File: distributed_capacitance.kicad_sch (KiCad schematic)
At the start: 22 parts

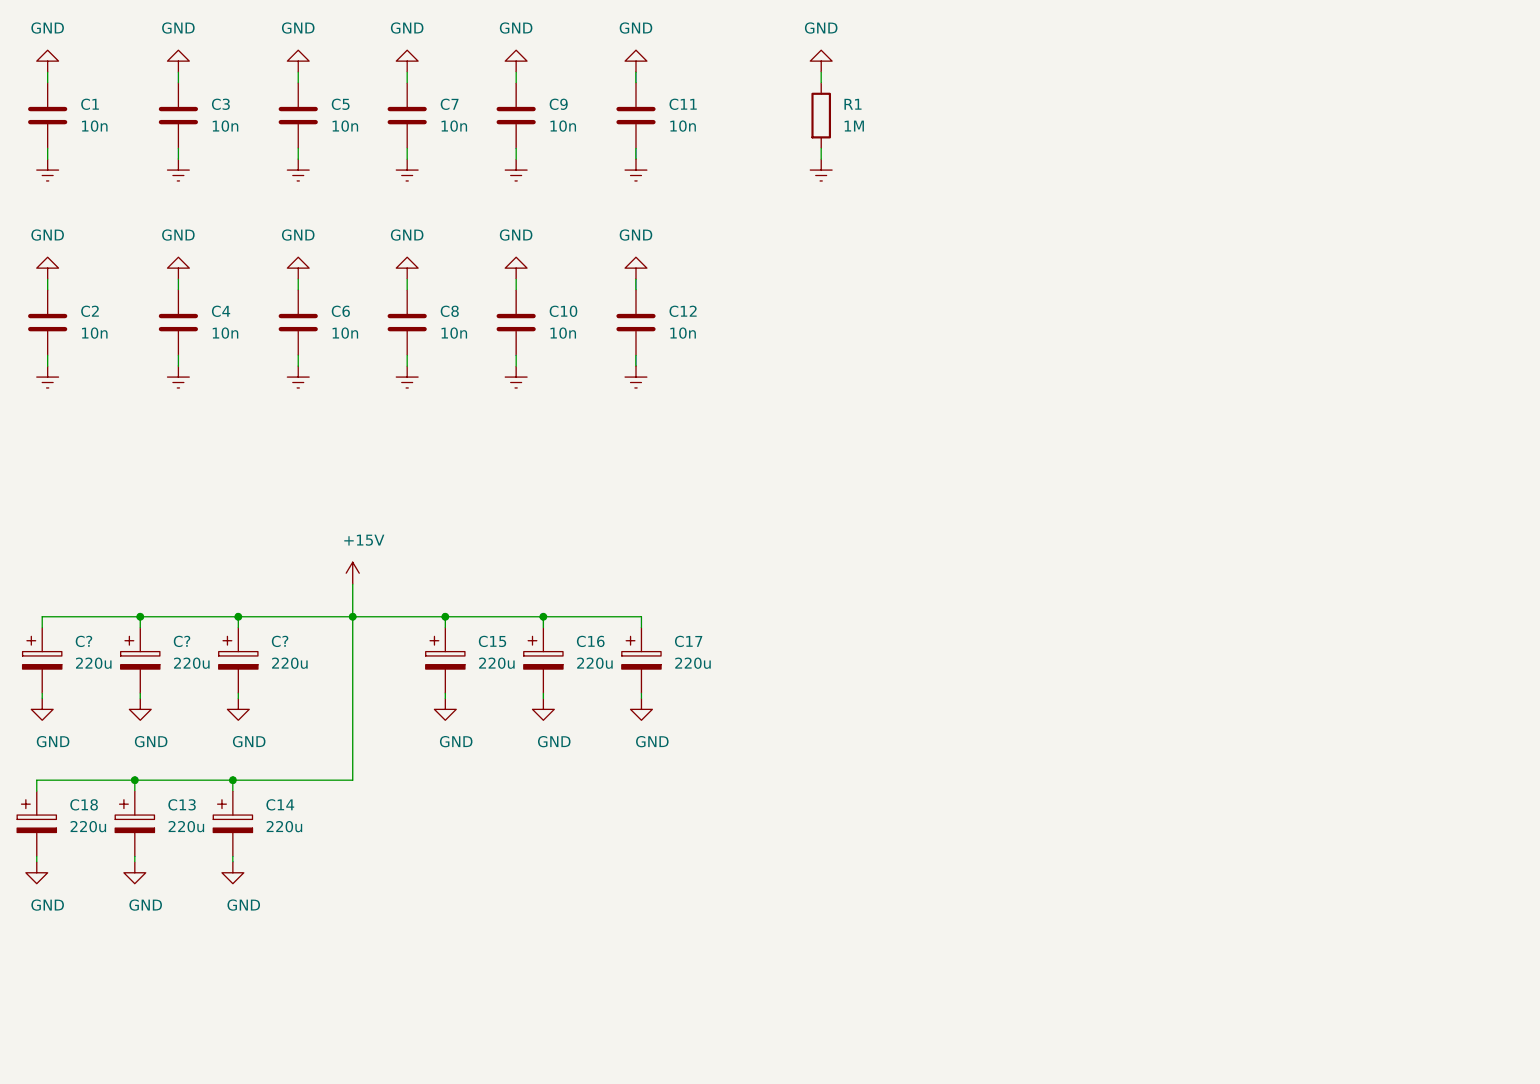
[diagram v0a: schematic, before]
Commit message: Added an input protection circuit Added CI
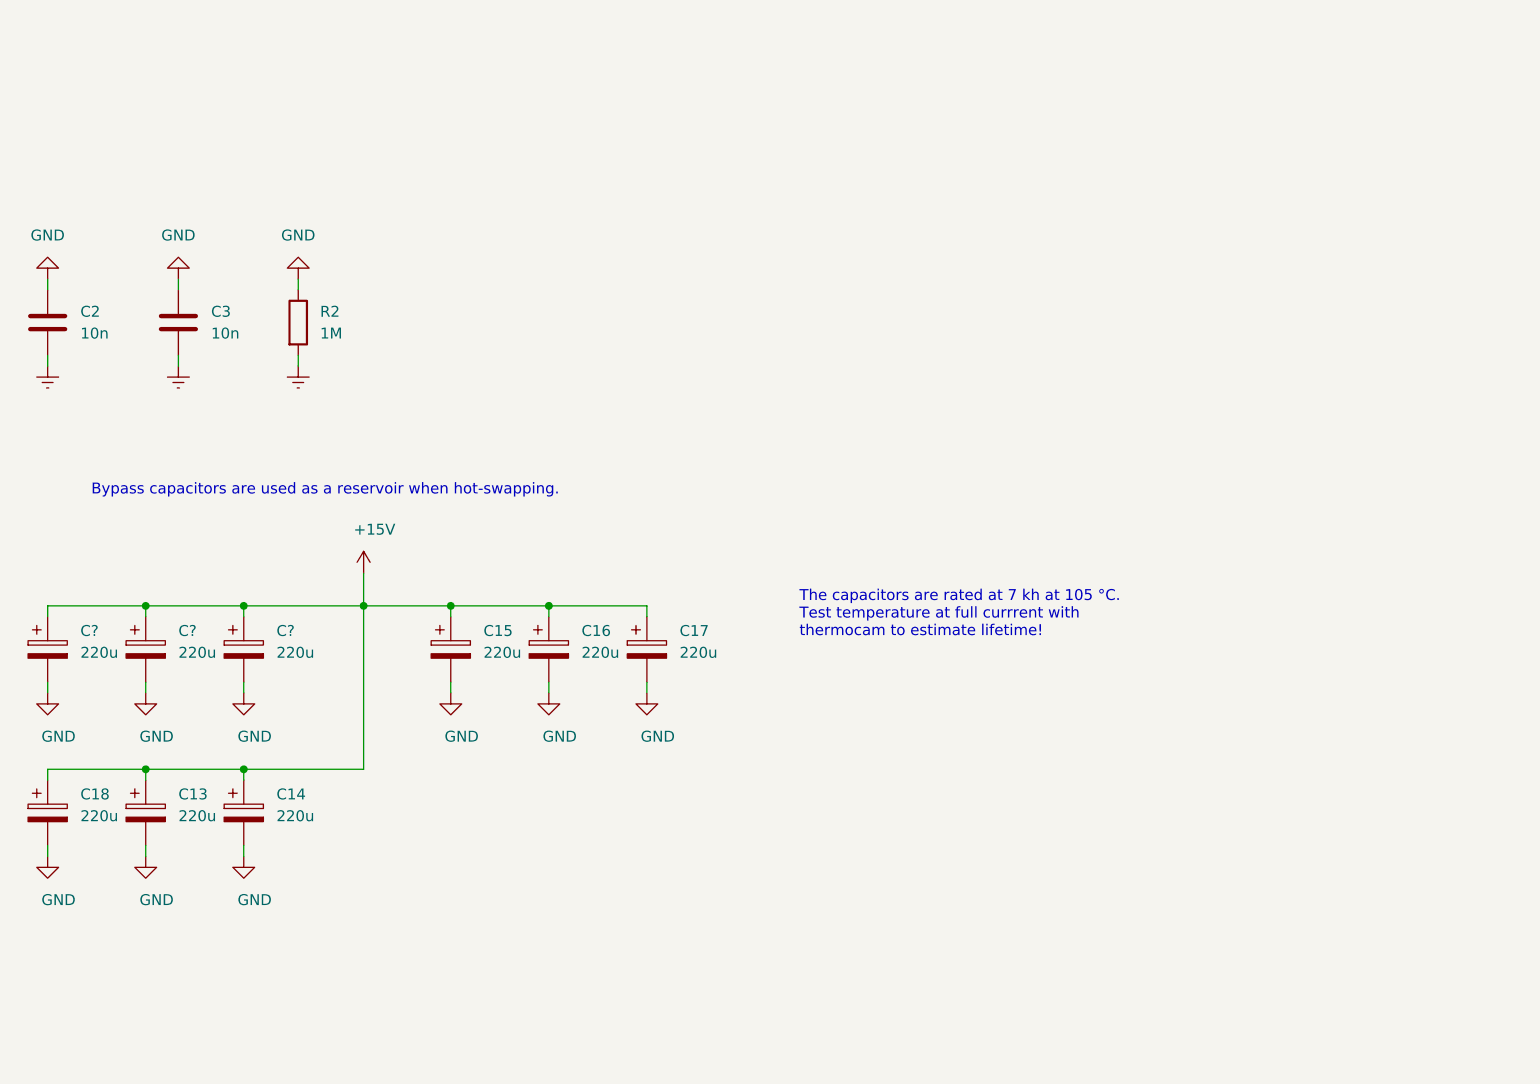
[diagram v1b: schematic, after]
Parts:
- removed C1, C10, C11, C12, C3, C5, C6, C7, C8, C9: 10n, Capacitor_SMD:C_0603_1608Metric, symbol Device:C
- C13, C14, C15, C16, C17, C18, C? (x3): RoHS (none) -> Yes; Temperature (none) -> Tstorage = –40 °C to 105 °C
- C2: Note 10n, 200V -> >= 200V; RoHS (none) -> Yes; Temperature (none) -> Tstorage = –55 °C to 155 °C; digikey# (none) -> 399-14191-1-ND
- C3: renamed from C4; Note 10n, 200V -> >= 200V; RoHS (none) -> Yes; Temperature (none) -> Tstorage = –55 °C to 155 °C; digikey# (none) -> 399-14191-1-ND
- R2: renamed from R1; RoHS (none) -> By exemption; Temperature (none) -> Tstorage = –55 °C to 155 °C
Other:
- note added: "Bypass capacitors are used as a reservoir when hot-swapping."
- note added: "The capacitors are rated at 7 kh at 105 °C. Test temperature at full currrent with thermocam to estimate lifetime!"
- title: 19" DIN 41612 Backplane -> Bypass capacitors
- moved on the sheet: C13, C14, C15, C16, C17, C18, C?, R2

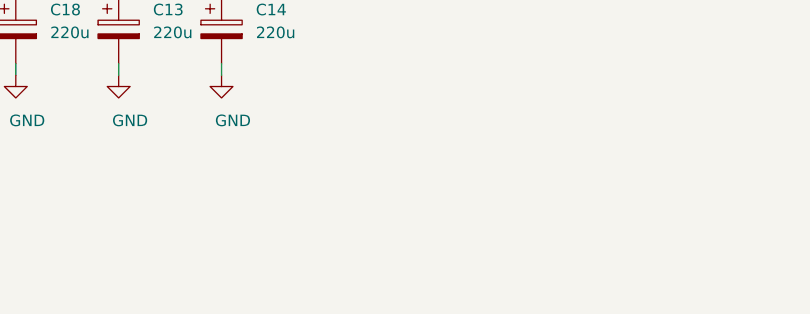
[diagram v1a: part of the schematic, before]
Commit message: Added Ferrite beads at the board input Moved power connector silkscreen labels Added TODO list for v.2.1.0
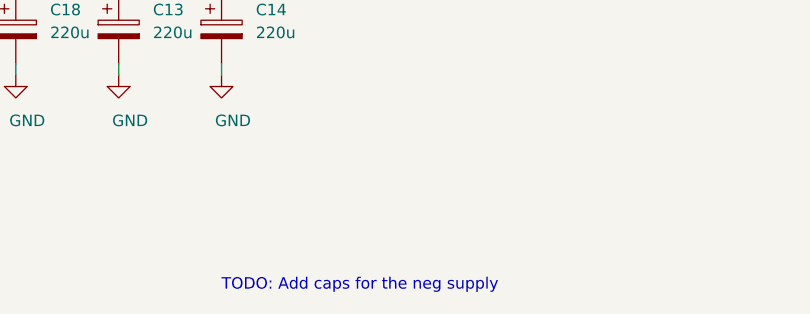
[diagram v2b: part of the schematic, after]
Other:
- note added: "TODO: Add caps for the neg supply"
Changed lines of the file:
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@@
     (stroke (width 0) (type default))
+  )
+  (text "TODO: Add caps for the neg supply" (at 66.04 149.86 0)
+    (effects (font (size 1.27 1.27)) (justify left bottom))
   )
   (text "The capacitors are rated at 7 kh at 105 °C.\nTest temperature at full currrent with\nthermocam to estimate lifetime!"

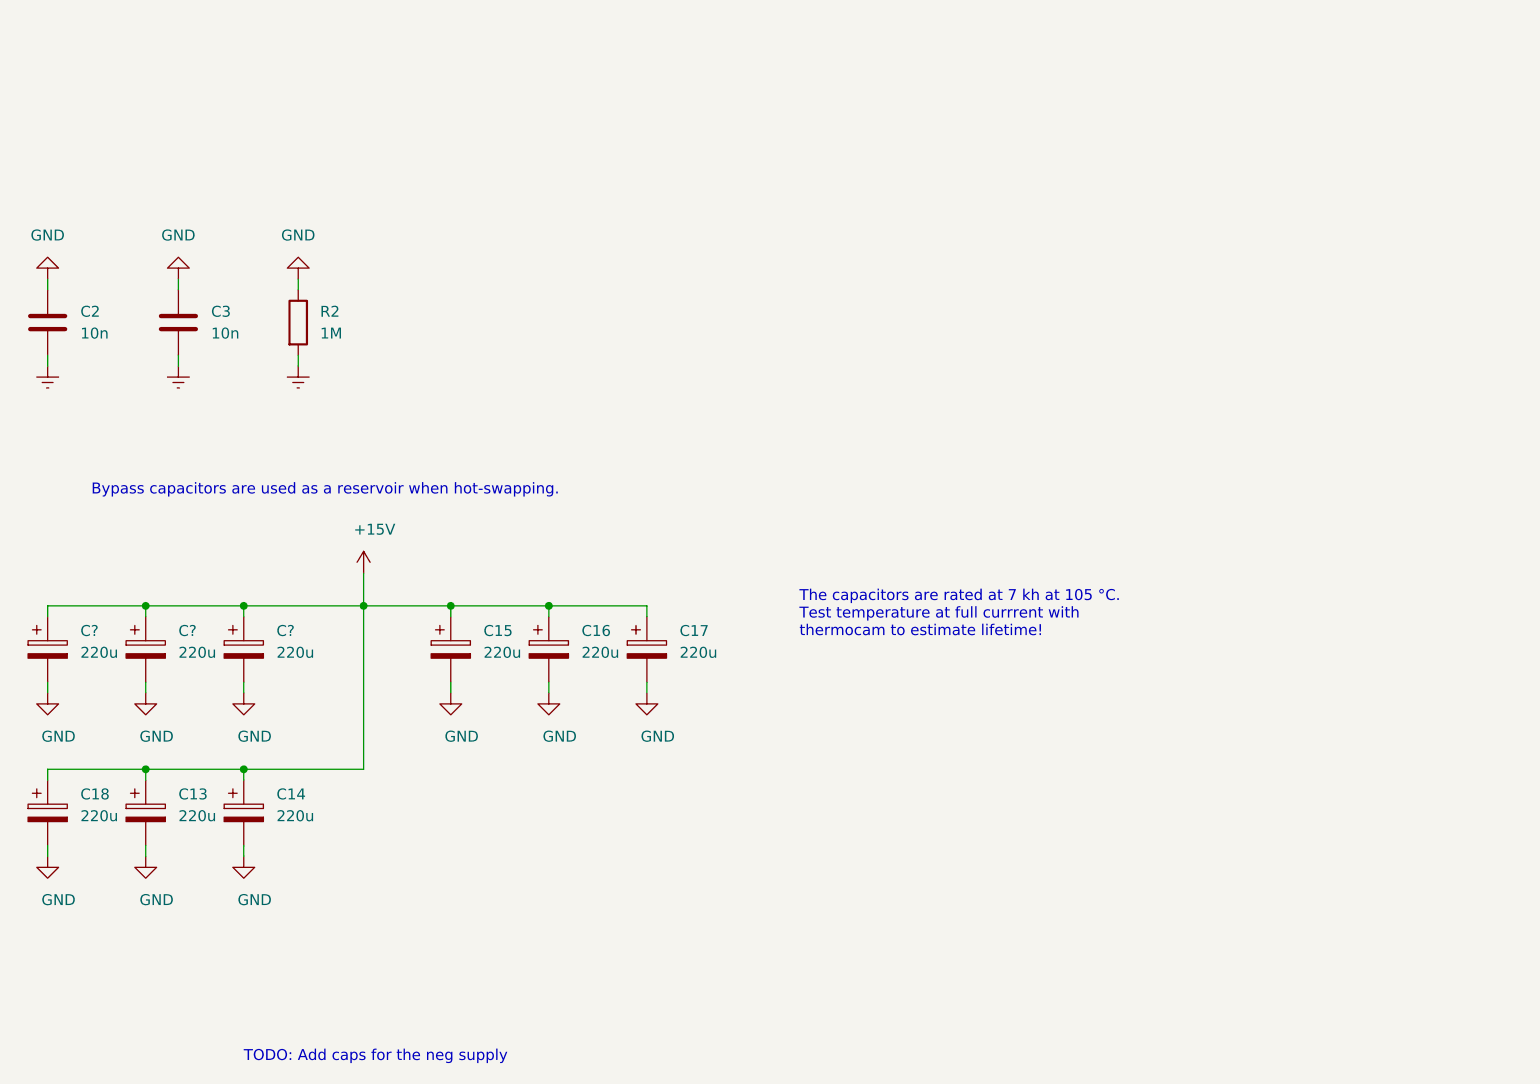
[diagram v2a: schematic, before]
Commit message: Replaced negative side NMOS with SQJQ160E Reduced number of thermal spokes required to 1
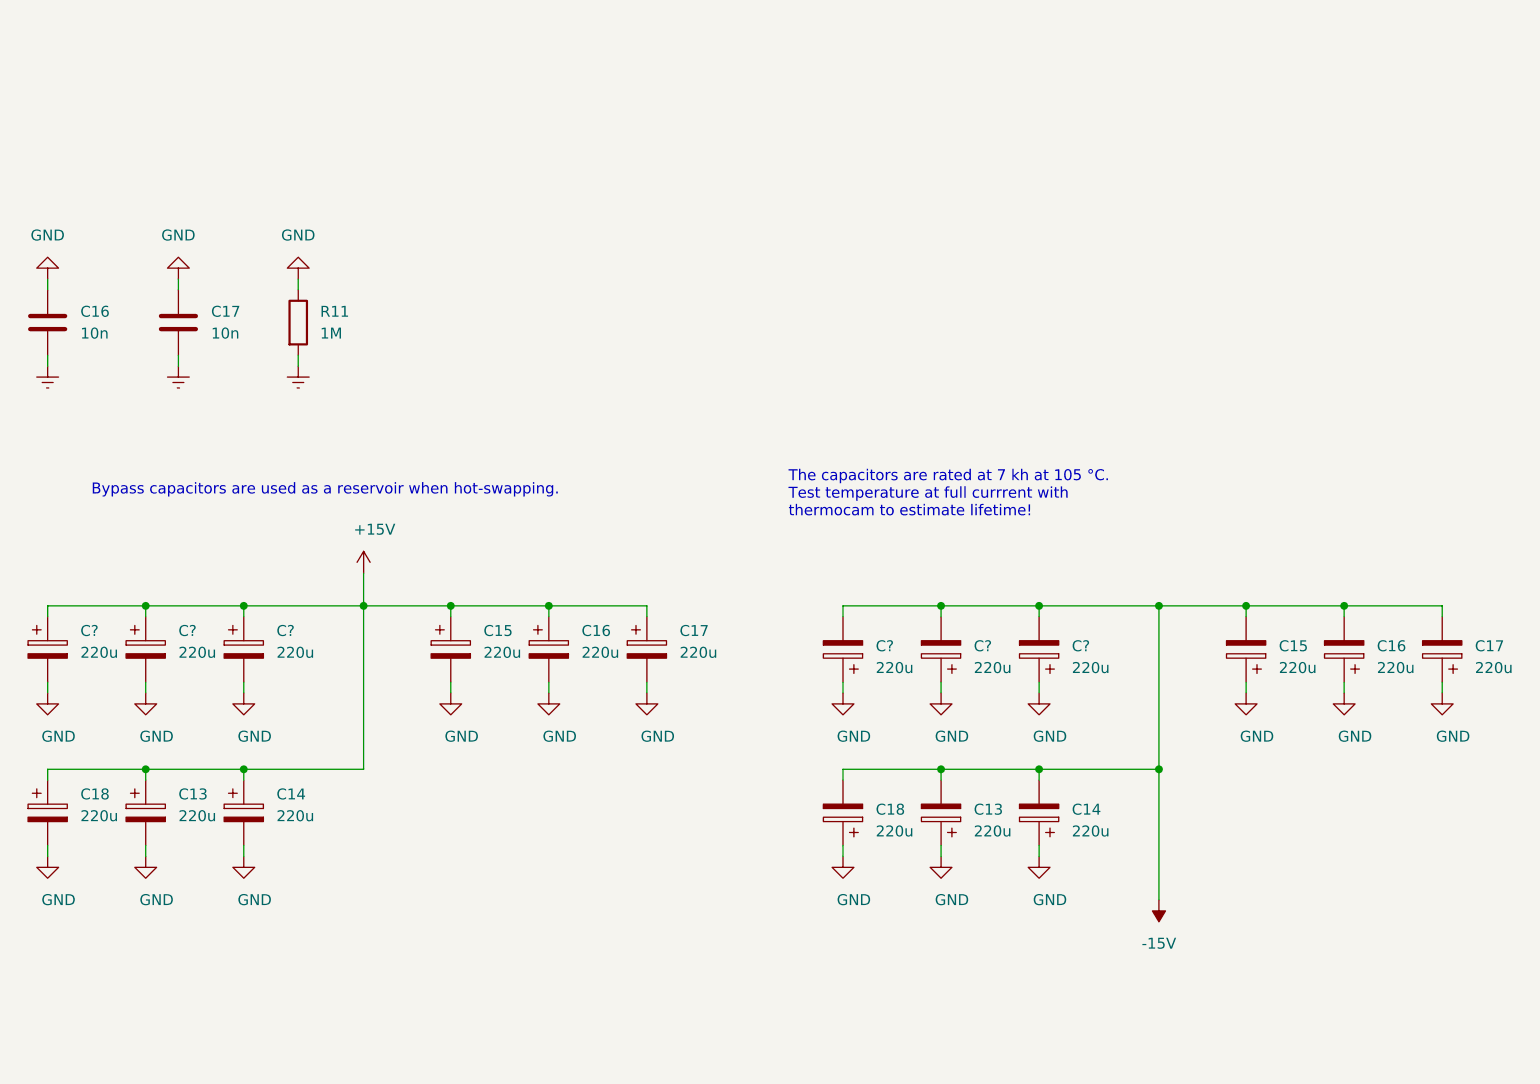
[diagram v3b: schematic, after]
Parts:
- added C13, C14, C15, C16, C17, C18, C? (x3): 220u, Capacitor_THT:CP_Radial_D8.0mm_P3.50mm, symbol Device:C_Polarized
- renumbered C2 to C16, C3 to C17, R2 to R11
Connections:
- net GND: now also C13.1, C14.1, C15.1, C16.1, C17.1, C18.1, C?.1, C?.1, C?.1
- new net -15V: C13.2, C14.2, C15.2, C16.2, C17.2, C18.2, C?.2, C?.2, C?.2
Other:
- note removed: "TODO: Add caps for the neg supply"
